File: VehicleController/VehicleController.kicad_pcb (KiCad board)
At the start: 4 copper layers, 127 x 68.6 mm, 150 parts, among them J1 CONN_02X05, J10 CONN_01X12, J11 RPI_PWR, J2 USF_SLAVE_I2C, J5 I2C_0, J6 I2C_1, J7 CAN_SER, J8 CONN_01X03, J9 CONN_01X12, P1 OUTPUTS, P2 OUTPUTS, P4 CONN_01X02, P5 CONN_02X04, Q1 Q_NMOS_GSD, Q2 Q_NMOS_GSD, Q3 Q_NMOS_GSD, Q4 Q_PMOS_GSD, Q5 Q_NMOS_GSD, Q6 Q_NMOS_GSD, Q7 Q_NMOS_GSD, U1 BTS4130QGA, U10 BTS6133D, U11 R-78E5.0-1.0, U12 FGMMOPA6H, U13 U.FL_Antenna, U14 NDC7002N, U15 MCP2551, U16 MC_Override, U17 MCR_Shtdwn, U18 MCL_Shtdwn, U19 RI-0505S, U2 BTS4130QGA, U20 ISO1540, U21 TCMT1103, U22 OPTO-TRANSISTOR-4, U23 PC_RLY, U24 MCP47FEBX2, U25 V7805W-2000, U3 BTS6133D, U4 BTS6133D, U5 H3LIS331DL, U6 UltimateSensorFusion, U7 Teensy_3.5, U8 NDC7003P, U9 TL431

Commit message: Routing changed
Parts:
- J10, J9: footprint UNCAMotorsports:MX120G-12 -> Connectors_Molex:Molex_NanoFit_2x06x2.50mm_Straight
- moved D4 32.0 mm to (93.0, 101.9)
- moved D3 31.8 mm to (93.0, 98.2)
- moved R19 30.7 mm to (65.7, 168.5)
- moved D2 22.1 mm to (58.2, 155.4)
- moved R20 22.0 mm to (63.6, 157.6)
- moved R23 21.0 mm to (92.8, 101.9)
- moved R22 20.4 mm to (92.3, 98.2)
- moved Q7 1.67 mm to (105.7, 85.7)
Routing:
- net GND: track 134.8 -> 179.5 mm, vias 19 -> 25
- net /GPS/VBACKUP: track 0.00 -> 37.5 mm, vias 0 -> 2
- net /SHTDWN_SIG: track 0.00 -> 36.9 mm
- net +3V3: track 73.6 -> 96.7 mm, vias 2 -> 3
- net Net-(U12-Pad11): track 0.00 -> 18.1 mm, vias 0 -> 2
- net Net-(Q7-Pad1): track 0.00 -> 17.9 mm, vias 0 -> 2
- net +12V: track 106.3 -> 91.0 mm
- net /3D_FIX: track 0.00 -> 13.0 mm, vias 0 -> 3
- net /MC_SHUTDOWN: track 10.7 -> 22.2 mm
- net Net-(D4-Pad2): track 9.45 -> 0.00 mm, vias 1 -> 0
- net Net-(D3-Pad2): track 9.37 -> 0.00 mm, vias 1 -> 0
- net Net-(D2-Pad1): track 8.76 -> 0.00 mm
- net /Isolation/KSI: track 92.7 -> 100.5 mm
- net Net-(Q1-Pad3): track 0.00 -> 7.61 mm
- net /GPS_RST: track 0.00 -> 7.16 mm, vias 0 -> 1
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
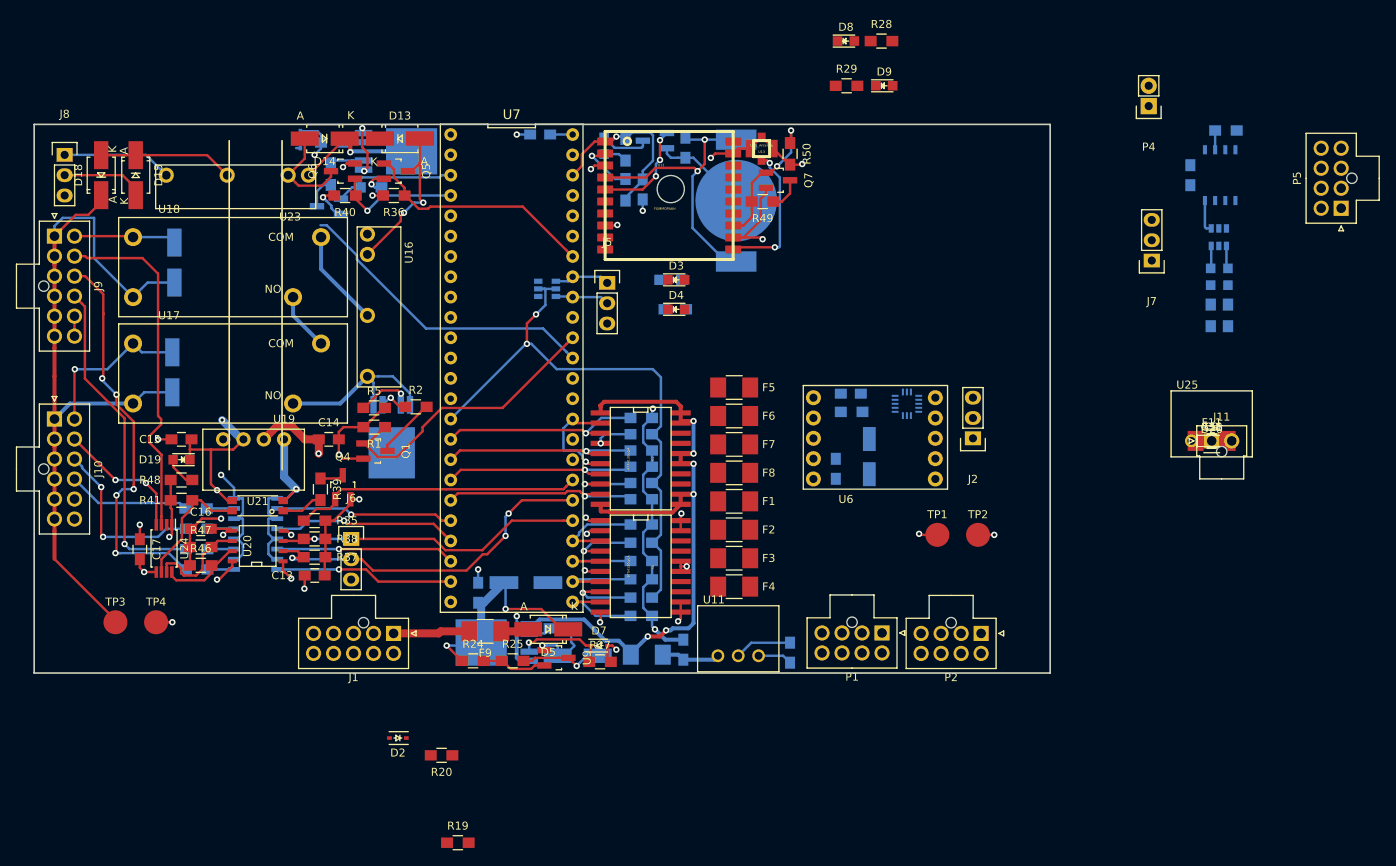
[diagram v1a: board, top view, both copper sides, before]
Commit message: Major VCU Layout changes
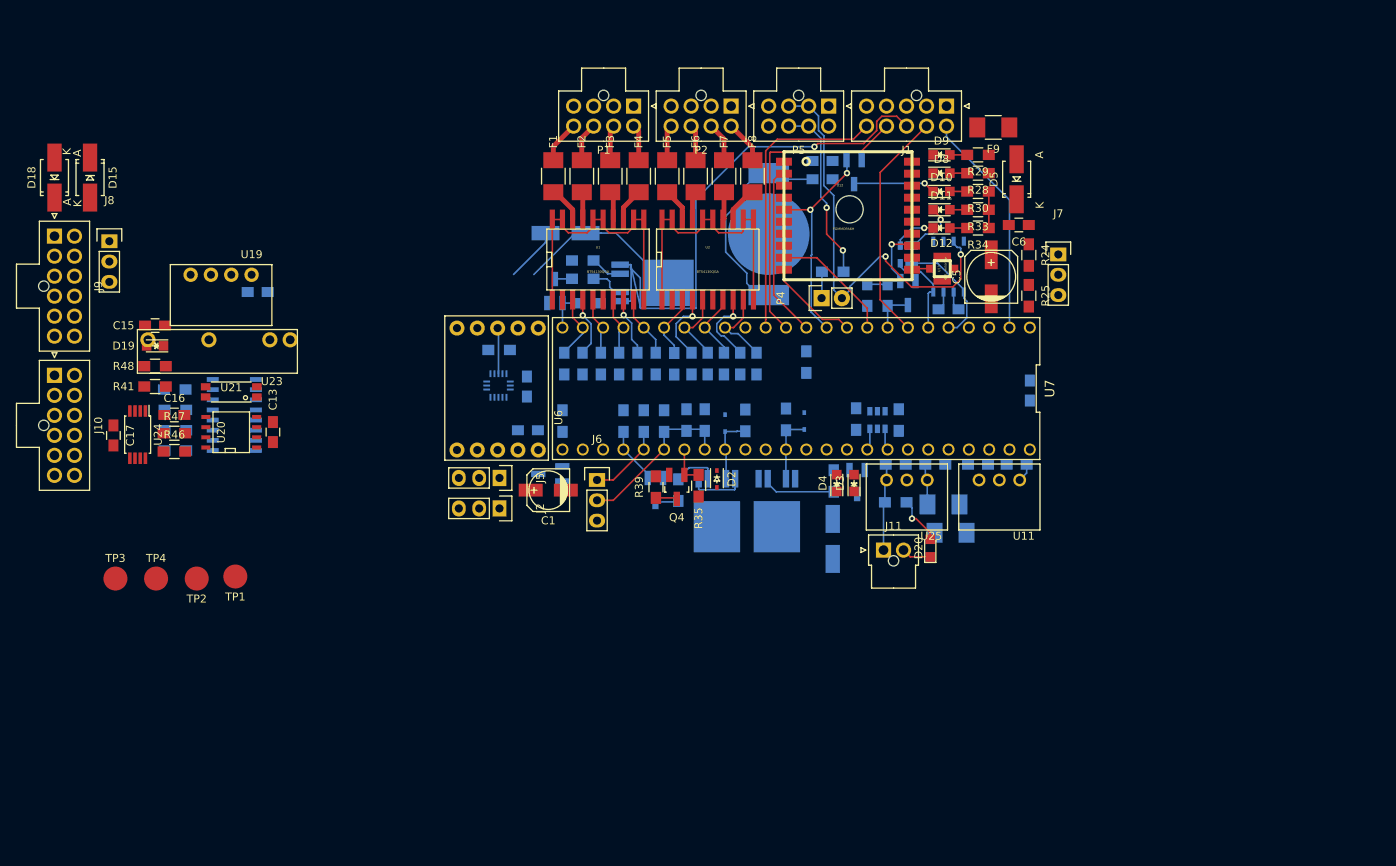
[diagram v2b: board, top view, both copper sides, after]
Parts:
- removed D13: D, Diodes_SMD:SMA_Handsoldering
- removed D16, D17: 1N4001, Diodes_SMD:SMA_Handsoldering
- removed Q5: Q_NMOS_GSD, TO_SOT_Packages_SMD:SOT-23_Handsoldering
- removed R36: 10k, Resistors_SMD:R_0805_HandSoldering
- removed U16: MC_Override, UNCAMotorsports:G6DN-1A
- removed U17: MCR_Shtdwn, UNCAMotorsports:ALE1PB48
- removed U18: MCL_Shtdwn, UNCAMotorsports:ALE1PB48
- C1, C5, C6, D10, D11, D12, R30, R33, R34: moved to F.Cu
- C14, C18, C9, D14, D7, F11, Q1, Q6, Q7, R1, R19, R2, R20, R27, R37, R38, R40, R49, R5, R50, R51, U9: moved to B.Cu
- F10: value 1A -> 3A
- F9: value 3A -> 5A
- moved TP2 97.8 mm to (33.0, 135.5), turned to 180 degrees
- moved J1 95.5 mm to (126.7, 76.5)
- moved F9 89.4 mm to (132.6, 79.1)
- moved TP1 87.9 mm to (37.8, 135.3), turned to 180 degrees
- moved R24 86.0 mm to (137.0, 95.1), turned to 270 degrees
- moved C6 81.7 mm to (135.8, 91.3), turned to 180 degrees
- moved D5 81.2 mm to (135.5, 85.6), turned to 90 degrees
- moved R25 79.0 mm to (137.0, 100.2), turned to 270 degrees
- moved P2 72.9 mm to (99.8, 76.5)
- moved P1 72.8 mm to (87.6, 76.5)
- moved C5 69.6 mm to (132.3, 97.8), turned to 90 degrees
- moved C4 69.1 mm to (137.2, 112.0), turned to 270 degrees
- moved P5 65.3 mm to (112.0, 76.5), turned to 180 degrees
- moved D1 63.8 mm to (99.1, 116.1)
- moved R19 60.1 mm to (94.2, 115.7), turned to 270 degrees
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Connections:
- D2 pad 1: Net-(D2-Pad1) -> /BATT_SENSE
- J1 pad 10: GND -> /AMS_F_OUT
- J1 pad 2: /START_CAR -> /TSMS
- J1 pad 4: /BRAKE_IN -> /SHTDWN_OUT
- J1 pad 5: /SHTDWN_OUT -> GND
- J1 pad 6: /IMD_F_OUT -> /START_CAR
- J1 pad 7: /TSMS -> /BRAKE_IN
- J1 pad 8: /AMS_F_OUT -> /AIR+
- J1 pad 9: /AIR+ -> /IMD_F_OUT
- P1 pad 1: Net-(F1-Pad1) -> GND
- P1 pad 2: Net-(F2-Pad1) -> GND
- P1 pad 3: Net-(F3-Pad1) -> GND
- P1 pad 4: Net-(F4-Pad1) -> GND
- P1 pad 5: GND -> Net-(F4-Pad1)
- P1 pad 6: GND -> Net-(F3-Pad1)
- P1 pad 7: GND -> Net-(F2-Pad1)
- P1 pad 8: GND -> Net-(F1-Pad1)
- P2 pad 1: Net-(F5-Pad1) -> GND
- P2 pad 2: Net-(F6-Pad1) -> GND
- P2 pad 3: Net-(F7-Pad1) -> GND
- P2 pad 4: Net-(F8-Pad1) -> GND
- P2 pad 5: GND -> Net-(F8-Pad1)
- P2 pad 6: GND -> Net-(F7-Pad1)
- P2 pad 7: GND -> Net-(F6-Pad1)
- P2 pad 8: GND -> Net-(F5-Pad1)
- R19 pad 2: Net-(D2-Pad1) -> /BATT_SENSE
- R20 pad 1: Net-(D2-Pad1) -> /BATT_SENSE
- U12 pad 14: (no net) -> Net-(U12-Pad14)
- U12 pad 15: (no net) -> Net-(U12-Pad15)
- U12 pad 16: (no net) -> Net-(U12-Pad16)
- U12 pad 17: (no net) -> Net-(U12-Pad17)
- U12 pad 18: (no net) -> Net-(U12-Pad18)
- U12 pad 20: (no net) -> Net-(U12-Pad20)
- U12 pad 6: (no net) -> Net-(U12-Pad6)
- U12 pad 7: (no net) -> Net-(U12-Pad7)
- U14 pad 1: /CANRX -> /CANTX
- U14 pad 3: /CANTX -> /CANRX
- U15 pad 5: (no net) -> Net-(U15-Pad5)
- U24 pad 2: (no net) -> Net-(U24-Pad2)
- U24 pad 6: /Isolation/LATCH_ISO -> GNDA
- U5 pad 2: (no net) -> Net-(U5-Pad2)
- U5 pad 3: (no net) -> Net-(U5-Pad3)
- U6 pad 3: (no net) -> Net-(U6-Pad3)
- U7 pad 16: /12VOUT0 -> /12VOUT3
- U7 pad 17: /12VOUT1 -> /12VOUT2
- U7 pad 18: /12VOUT2 -> /12VOUT1
- U7 pad 19: /12VOUT3 -> /12VOUT0
- U7 pad 20: /Isolation/F_R2 -> /5VOUT3
- U7 pad 21: /Isolation/F_R1 -> /5VOUT2
- U7 pad 22: /Isolation/F_L2 -> /5VOUT1
- U7 pad 23: /Isolation/F_L1 -> /5VOUT0
- U7 pad 24: Net-(D2-Pad1) -> /CLOSE_AIR
- U7 pad 25: /5VOUT3 -> /PC_CTRL
- U7 pad 26: /5VOUT2 -> /MC_OVERRIDE
- U7 pad 27: /5VOUT1 -> /IMU_INT
- U7 pad 28: /5VOUT0 -> /SHTDWN_SIG
- U7 pad 3: /CLOSE_AIR -> Net-(U7-Pad3)
- U7 pad 32: (no net) -> /BATT_SENSE
- U7 pad 33: (no net) -> /SHTDWN_CURRENT
- U7 pad 35: (no net) -> Net-(U7-Pad35)
- U7 pad 37: /SHTDWN_CURRENT -> Net-(U7-Pad37)
- U7 pad 38: /SHTDWN_SIG -> Net-(U7-Pad38)
- U7 pad 39: /IMU_INT -> Net-(U7-Pad39)
- U7 pad 4: /PC_CTRL -> Net-(U7-Pad4)
- U7 pad 42: /MC_OVERRIDE -> Net-(U7-Pad42)
- U7 pad 43: (no net) -> Net-(U7-Pad43)
- U7 pad 44: (no net) -> Net-(U7-Pad44)
- U7 pad 45: (no net) -> Net-(U7-Pad45)
- U7 pad 47: (no net) -> Net-(U7-Pad47)
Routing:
- net GND: track 179.5 -> 6.11 mm, vias 25 -> 0
- net /Isolation/KSI: track 100.5 -> 0.00 mm
- net +3V3: track 96.7 -> 4.57 mm, vias 3 -> 0
- net /AIR+: track 6.70 -> 71.1 mm, vias 2 -> 1
- net +12V: track 91.0 -> 36.8 mm, vias 7 -> 0
- net /CAN Bus/CANH: track 0.32 -> 53.1 mm, vias 0 -> 2
- net /Isolation/FAULT_L1: track 50.2 -> 0.00 mm, vias 5 -> 0
- net GNDA: track 49.1 -> 0.00 mm, vias 6 -> 0
- net /Isolation/DAC_L: track 44.5 -> 0.00 mm
- net /Isolation/FAULT_L2: track 41.9 -> 0.00 mm, vias 1 -> 0
- net /IMD_F_OUT: track 0.00 -> 38.7 mm
- net /SHTDWN_CURRENT: track 46.4 -> 8.32 mm, vias 1 -> 0
- net /AMS_F_OUT: track 0.00 -> 36.0 mm
- net /DAC_LATCH: track 36.3 -> 4.95 mm
- net /SDA1: track 45.3 -> 15.3 mm, vias 3 -> 0
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- removed copper zone on PWR, net +5V
- removed copper zone on PWR, net +5VA
- removed copper zone on GND, net GND
- removed copper zone on GND, net GNDA
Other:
- board size 127 x 68.6 mm -> 3.4 x 3.4 mm
- net class Default: clearance 0.2032 -> 0.1778; trace_width 0.3048 -> 0.2032
- rule trace_clearance: 0.2032 -> 0.1778

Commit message: Finish VCU 4 layer
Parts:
- added G***: LOGO, UNCAMotorsports:UNCA Logo, F.Cu at (54.0, 127.0)
- added REF**: MountingHole_3mm, Mounting_Holes:MountingHole_3mm, F.Cu at (42.5, 75.6)
- added REF**: MountingHole_3mm, Mounting_Holes:MountingHole_3mm, F.Cu at (42.5, 126.4)
- added REF**: MountingHole_3mm, Mounting_Holes:MountingHole_3mm, F.Cu at (135.3, 75.6)
- added REF**: MountingHole_3mm, Mounting_Holes:MountingHole_3mm, F.Cu at (93.3, 126.4)
- C15, D20, D5, F9: moved to B.Cu
- moved GND 66.1 mm to (71.2, 81.5), turned to 0 degrees
- moved +5v 59.5 mm to (71.2, 86.0), turned to 0 degrees
- moved U3 44.0 mm to (91.6, 85.5), turned to 90 degrees
- moved Q1 42.2 mm to (78.8, 83.8), turned to 90 degrees
- moved R2 40.2 mm to (79.6, 86.6), turned to 180 degrees
- moved R35 39.3 mm to (66.2, 98.0), turned to 180 degrees
- moved R39 37.2 mm to (66.2, 95.8), turned to 180 degrees
- moved KSI 35.7 mm to (54.6, 119.3), turned to 90 degrees
- moved Q4 35.6 mm to (71.4, 95.8), turned to 90 degrees
- moved C17 34.3 mm to (52.6, 101.0), turned to 180 degrees
- moved J10 33.8 mm to (42.7, 90.4)
- moved C15 33.5 mm to (54.8, 84.1)
- moved J9 31.4 mm to (42.7, 108.0)
- moved J8 31.1 mm to (50.5, 80.8)
- moved U10 30.5 mm to (132.3, 114.6), turned to 90 degrees
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- renumbered TP1 to +5v, TP2 to GND, TP4 to GNDA, TP3 to KSI
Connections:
- net /MC_OVERRIDE renamed Net-(U7-Pad26)
- J1 pad 10: /AMS_F_OUT -> /GLVMS
- J1 pad 2: /TSMS -> /IMD_F_OUT
- J1 pad 3: /GLVMS -> /AMS_F_OUT
- J1 pad 4: /SHTDWN_OUT -> /SHUTDOWN_OUT
- J1 pad 8: /AIR+ -> /TSMS
- J1 pad 9: /IMD_F_OUT -> /AIR+
- J10 pad 10: /Isolation/FAULT_R2 -> /Isolation/FAULT_R1
- J10 pad 9: /Isolation/FAULT_R1 -> /Isolation/FAULT_R2
- J9 pad 10: /Isolation/FAULT_L2 -> /Isolation/FAULT_L1
- J9 pad 9: /Isolation/FAULT_L1 -> /Isolation/FAULT_L2
- U22 pad 10: /Isolation/F_R2 -> /F_R2
- U22 pad 12: /Isolation/F_R1 -> /F_R1
- U22 pad 14: /Isolation/F_L2 -> /F_L2
- U22 pad 16: /Isolation/F_L1 -> /F_L1
- U3 pad 1: /MC_SHUTDOWN -> /SHUTDOWN_OUT
- U3 pad 5: /MC_SHUTDOWN -> /SHUTDOWN_OUT
- U7 pad 35: Net-(U7-Pad35) -> /GLV_CURRENT
- U7 pad 36: /GLV_CURRENT -> /F_L1
- U7 pad 37: Net-(U7-Pad37) -> /F_L2
- U7 pad 38: Net-(U7-Pad38) -> /F_R1
- U7 pad 39: Net-(U7-Pad39) -> /F_R2
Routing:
- net GND: track 6.11 -> 237.8 mm, vias 0 -> 31
- net +3V3: track 4.57 -> 177.2 mm, vias 0 -> 14
- net +12V: track 36.8 -> 168.5 mm, vias 0 -> 3
- net /F_R2: track 0.00 -> 79.7 mm
- net /F_R1: track 0.00 -> 70.8 mm
- net /F_L2: track 0.00 -> 64.8 mm
- net /SCL0: track 3.43 -> 68.1 mm, vias 0 -> 1
- net /SDA0: track 3.43 -> 66.4 mm
- net /F_L1: track 0.00 -> 56.8 mm
- net /TSMS: track 21.5 -> 72.5 mm, vias 0 -> 4
- net /SHTDWN_SIG: track 7.02 -> 57.9 mm, vias 0 -> 2
- net /SHUTDOWN_OUT: track 0.00 -> 47.2 mm, vias 0 -> 2
- net Net-(C5-Pad1): track 0.10 -> 41.7 mm, vias 0 -> 3
- net /SHTDWN_CURRENT: track 8.32 -> 47.9 mm, vias 0 -> 1
- net Net-(J2-Pad2): track 0.00 -> 38.9 mm
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- added copper zone on PWR, net +5V
- added copper zone on PWR, net /Isolation/KSI
- added copper zone on GND, net GND
- added copper zone on GND, net GNDA
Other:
- board size 3.4 x 3.4 mm -> 99.1 x 57.1 mm
- board text added: "HIGH VOLTAGE"
- board text added: "UNCA 2017 Vehicle Control Unit June 2, 2017 Paul Guenette Patrick Johnson"

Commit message: VCU Finalization, BOM generation
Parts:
- moved U19 0.51 mm to (63.3, 81.3)
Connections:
- U7 pad 36: /F_L1 -> /F_R2
- U7 pad 37: /F_L2 -> /F_R1
- U7 pad 38: /F_R1 -> /F_L2
- U7 pad 39: /F_R2 -> /F_L1
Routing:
- net /F_R2: track 79.7 -> 65.3 mm
- net /F_L1: track 56.8 -> 70.2 mm
- net GND: track 237.8 -> 232.3 mm, vias 31 -> 32
- net /F_R1: track 70.8 -> 66.5 mm
- net /F_L2: track 64.8 -> 67.5 mm
- net +5V: track 74.1 -> 73.4 mm
- net /Isolation/FAULT_R2: track 8.65 -> 8.05 mm
- added copper zone on F.Cu, net +12V
- added copper zone on B.Cu, net +3V3
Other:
- rule via_min_size: 0.4 -> 0.6
- board text added: "Rev 02"
